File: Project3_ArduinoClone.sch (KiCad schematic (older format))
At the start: 0 parts

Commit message: Create new child sheet, added symbols
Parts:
- added BT?: Battery, symbol Device:Battery
- added C? (x2): C, symbol Device:C
- added C?: CP, symbol Device:CP
- added D?: LED, symbol Device:LED
- added R? (x2): R, symbol Device:R
- added U?: 24LC1025, symbol Memory_EEPROM:24LC1025
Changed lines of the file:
@@
 $Descr A4 11693 8268
 encoding utf-8
-Sheet 1 1
+Sheet 1 2
 Title "Arduino Clone (with clock and EEPROM)"
 Date "2021-04-17"
@@
 Comment4 ""
 $EndDescr
+$Comp
+L Device:Battery BT?
+U 1 1 607B6E62
+P 3200 2950
+F 0 "BT?" H 3308 2996 50  0000 L CNN
+F 1 "Battery" H 3308 2905 50  0000 L CNN
+F 2 "" V 3200 3010 50  0001 C CNN
+F 3 "~" V 3200 3010 50  0001 C CNN
+	1    3200 2950
+	1    0    0    -1
+$EndComp
+$Comp
+L Device:C C?
+U 1 1 607B7C54
+P 3975 2725
+F 0 "C?" H 4090 2771 50  0000 L CNN
+F 1 "C" H 4090 2680 50  0000 L CNN
+F 2 "" H 4013 2575 50  0001 C CNN
+F 3 "~" H 3975 2725 50  0001 C CNN
+	1    3975 2725
+	1    0    0    -1
+$EndComp
+$Comp
+L Device:C C?
+U 1 1 607B8169
+P 3975 3275
+F 0 "C?" H 4090 3321 50  0000 L CNN
+F 1 "C" H 4090 3230 50  0000 L CNN
+F 2 "" H 4013 3125 50  0001 C CNN
+F 3 "~" H 3975 3275 50  0001 C CNN
+	1    3975 3275
+	1    0    0    -1
+$EndComp
+$Comp
+L Device:CP C?
+U 1 1 607B88C0
+P 3975 3800
+F 0 "C?" H 4093 3846 50  0000 L CNN
+F 1 "CP" H 4093 3755 50  0000 L CNN
+F 2 "" H 4013 3650 50  0001 C CNN
+F 3 "~" H 3975 3800 50  0001 C CNN
+	1    3975 3800
+	1    0    0    -1
+$EndComp
+$Comp
+L Device:LED D?
+U 1 1 607B9296
+P 3200 3825
+F 0 "D?" H 3193 4042 50  0000 C CNN
+F 1 "LED" H 3193 3951 50  0000 C CNN
+F 2 "" H 3200 3825 50  0001 C CNN
+F 3 "~" H 3200 3825 50  0001 C CNN
+	1    3200 3825
+	1    0    0    -1
+$EndComp
+$Comp
+L Device:R R?
+U 1 1 607B9949
+P 4750 2750
+F 0 "R?" H 4820 2796 50  0000 L CNN
+F 1 "R" H 4820 2705 50  0000 L CNN
+F 2 "" V 4680 2750 50  0001 C CNN
+F 3 "~" H 4750 2750 50  0001 C CNN
+	1    4750 2750
+	1    0    0    -1
+$EndComp
+$Comp
+L Device:R R?
+U 1 1 607B9E3D
+P 4750 3300
+F 0 "R?" H 4820 3346 50  0000 L CNN
+F 1 "R" H 4820 3255 50  0000 L CNN
+F 2 "" V 4680 3300 50  0001 C CNN
+F 3 "~" H 4750 3300 50  0001 C CNN
+	1    4750 3300
+	1    0    0    -1
+$EndComp
+$Comp
+L Memory_EEPROM:24LC1025 U?
+U 1 1 607BB185
+P 5650 2825
+F 0 "U?" H 5650 3306 50  0000 C CNN
+F 1 "24LC1025" H 5650 3215 50  0000 C CNN
+F 2 "" H 5650 2825 50  0001 C CNN
+F 3 "http://ww1.microchip.com/downloads/en/DeviceDoc/21941B.pdf" H 5650 2825 50  0001 C CNN
+	1    5650 2825
+	1    0    0    -1
+$EndComp
+$Sheet
+S 5650 3750 2475 2350
+U 607BC0FB
+F0 "Connectors" 50
+F1 "Connectors.sch" 50
+$EndSheet
 $EndSCHEMATC

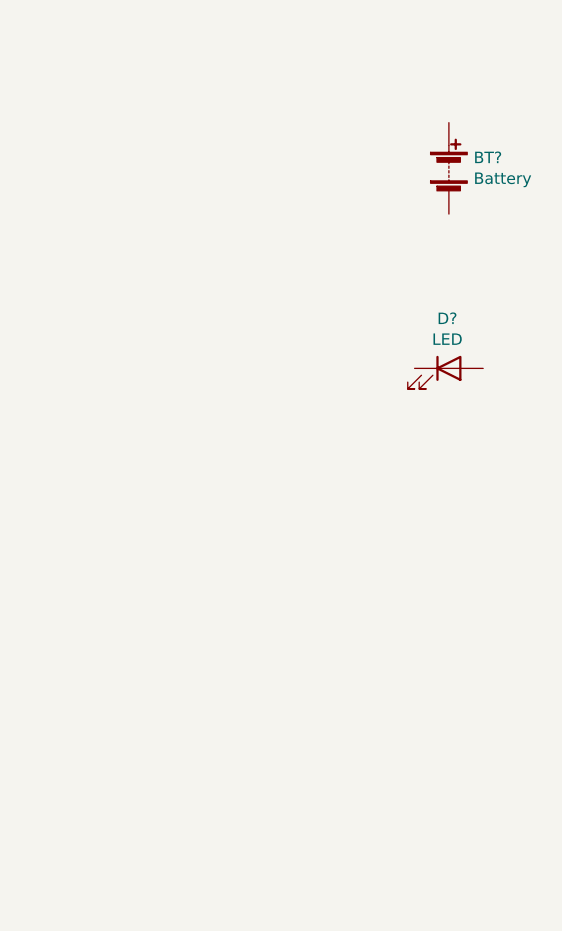
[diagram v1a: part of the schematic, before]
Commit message: Added symbol for atmega328p-au
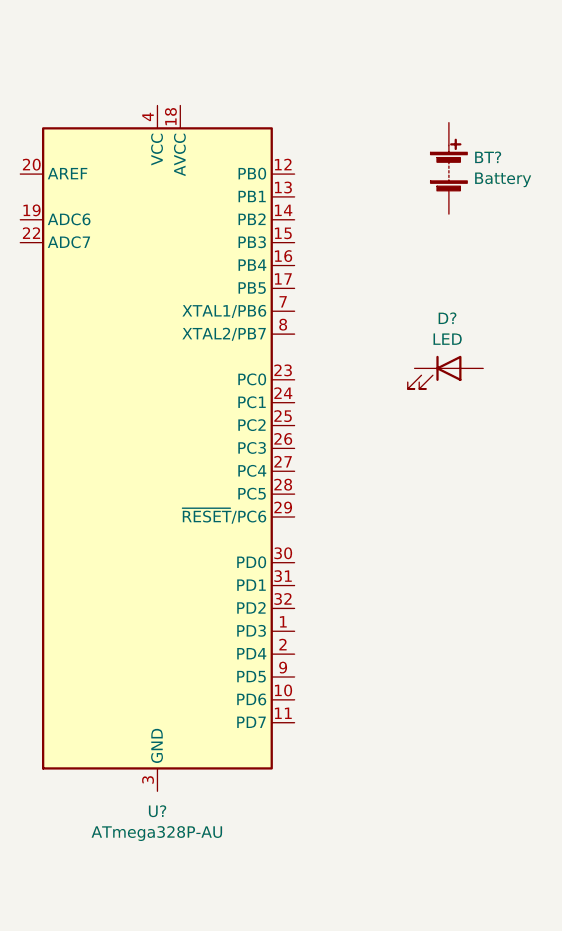
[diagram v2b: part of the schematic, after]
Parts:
- added U?: ATmega328P-AU, Package_QFP:TQFP-32_7x7mm_P0.8mm, symbol MCU_Microchip_ATmega:ATmega328P-AU
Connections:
- new net: U?.21 (GND), U?.3 (GND), U?.5 (GND)
- new net: U?.4 (VCC), U?.6 (VCC)
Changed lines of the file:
@@
 F1 "Connectors.sch" 50
 $EndSheet
+$Comp
+L MCU_Microchip_ATmega:ATmega328P-AU U?
+U 1 1 6086469A
+P 1925 4175
+F 0 "U?" H 1925 2586 50  0000 C CNN
+F 1 "ATmega328P-AU" H 1925 2495 50  0000 C CNN
+F 2 "Package_QFP:TQFP-32_7x7mm_P0.8mm" H 1925 4175 50  0001 C CIN
+F 3 "http://ww1.microchip.com/downloads/en/DeviceDoc/ATmega328_P%20AVR%20MCU%20with%20picoPower%20Technology%20Data%20Sheet%2040001984A.pdf" H 1925 4175 50  0001 C CNN
+	1    1925 4175
+	1    0    0    -1
+$EndComp
 $EndSCHEMATC

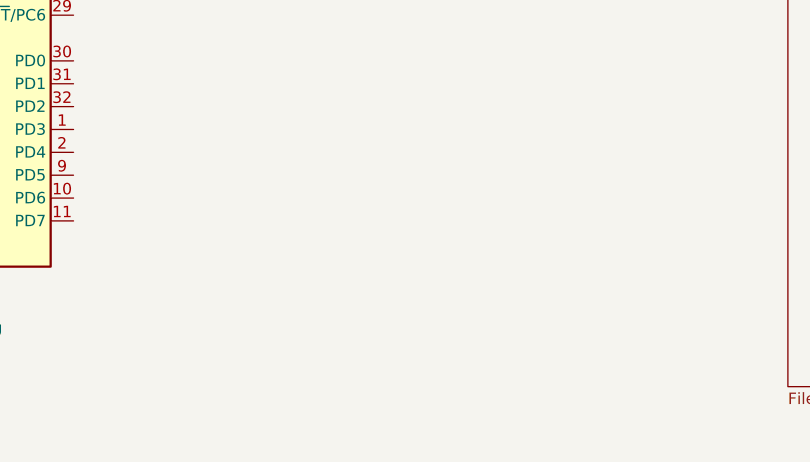
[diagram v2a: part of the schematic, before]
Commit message: Added clock IC custom symbol
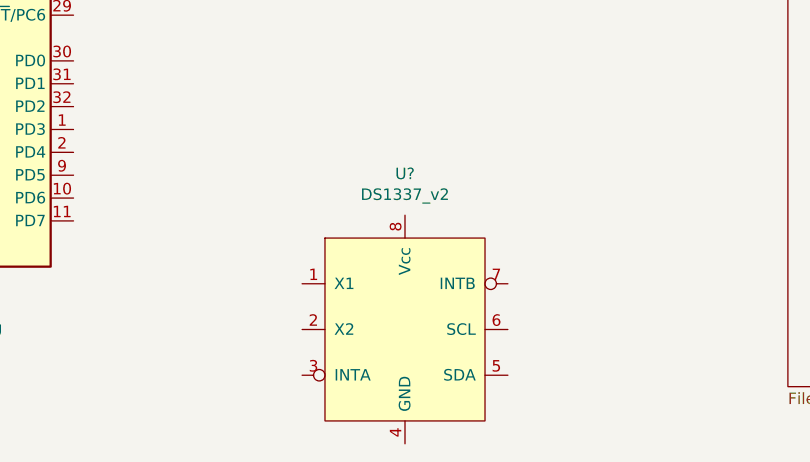
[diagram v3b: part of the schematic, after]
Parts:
- added U?: DS1337_v2, symbol project3:DS1337_v2
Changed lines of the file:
@@
+	1    0    0    -1
+$EndComp
+$Comp
+L project3:DS1337_v2 U?
+U 1 1 60E3C73A
+P 3975 5850
+F 0 "U?" H 3975 6531 50  0000 C CNN
+F 1 "DS1337_v2" H 3975 6440 50  0000 C CNN
+F 2 "" H 3975 5850 50  0001 C CNN
+F 3 "https://datasheets.maximintegrated.com/en/ds/DS1337-DS1337C.pdf" H 3975 5850 50  0001 C CNN
+	1    3975 5850
 	1    0    0    -1
 $EndComp

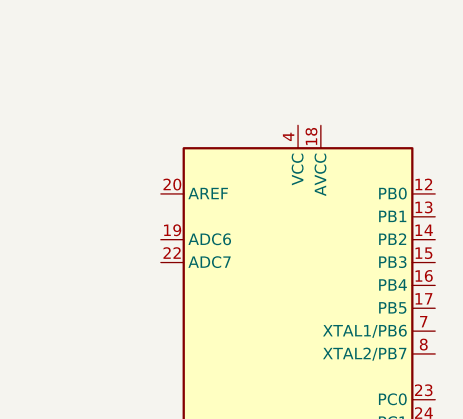
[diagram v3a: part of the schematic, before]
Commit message: added 2 crystals
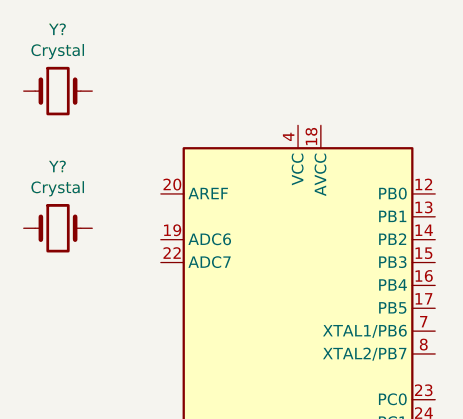
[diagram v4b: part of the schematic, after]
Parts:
- added Y? (x2): Crystal, symbol Device:Crystal
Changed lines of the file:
@@
+	1    0    0    -1
+$EndComp
+$Comp
+L Device:Crystal Y?
+U 1 1 60E3DE79
+P 875 2525
+F 0 "Y?" H 875 2793 50  0000 C CNN
+F 1 "Crystal" H 875 2702 50  0000 C CNN
+F 2 "" H 875 2525 50  0001 C CNN
+F 3 "~" H 875 2525 50  0001 C CNN
+	1    875  2525
+	1    0    0    -1
+$EndComp
+$Comp
+L Device:Crystal Y?
+U 1 1 60E3EBBC
+P 875 3125
+F 0 "Y?" H 875 3393 50  0000 C CNN
+F 1 "Crystal" H 875 3302 50  0000 C CNN
+F 2 "" H 875 3125 50  0001 C CNN
+F 3 "~" H 875 3125 50  0001 C CNN
+	1    875  3125
 	1    0    0    -1
 $EndComp
